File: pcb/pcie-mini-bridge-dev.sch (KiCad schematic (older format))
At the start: 20 parts, among them J1 Conn_01x02, J2 USB_C_Receptacle, J3 Conn_01x02, J4 Conn_01x02, J5 PCIe_x1, U1 TPS2594xx

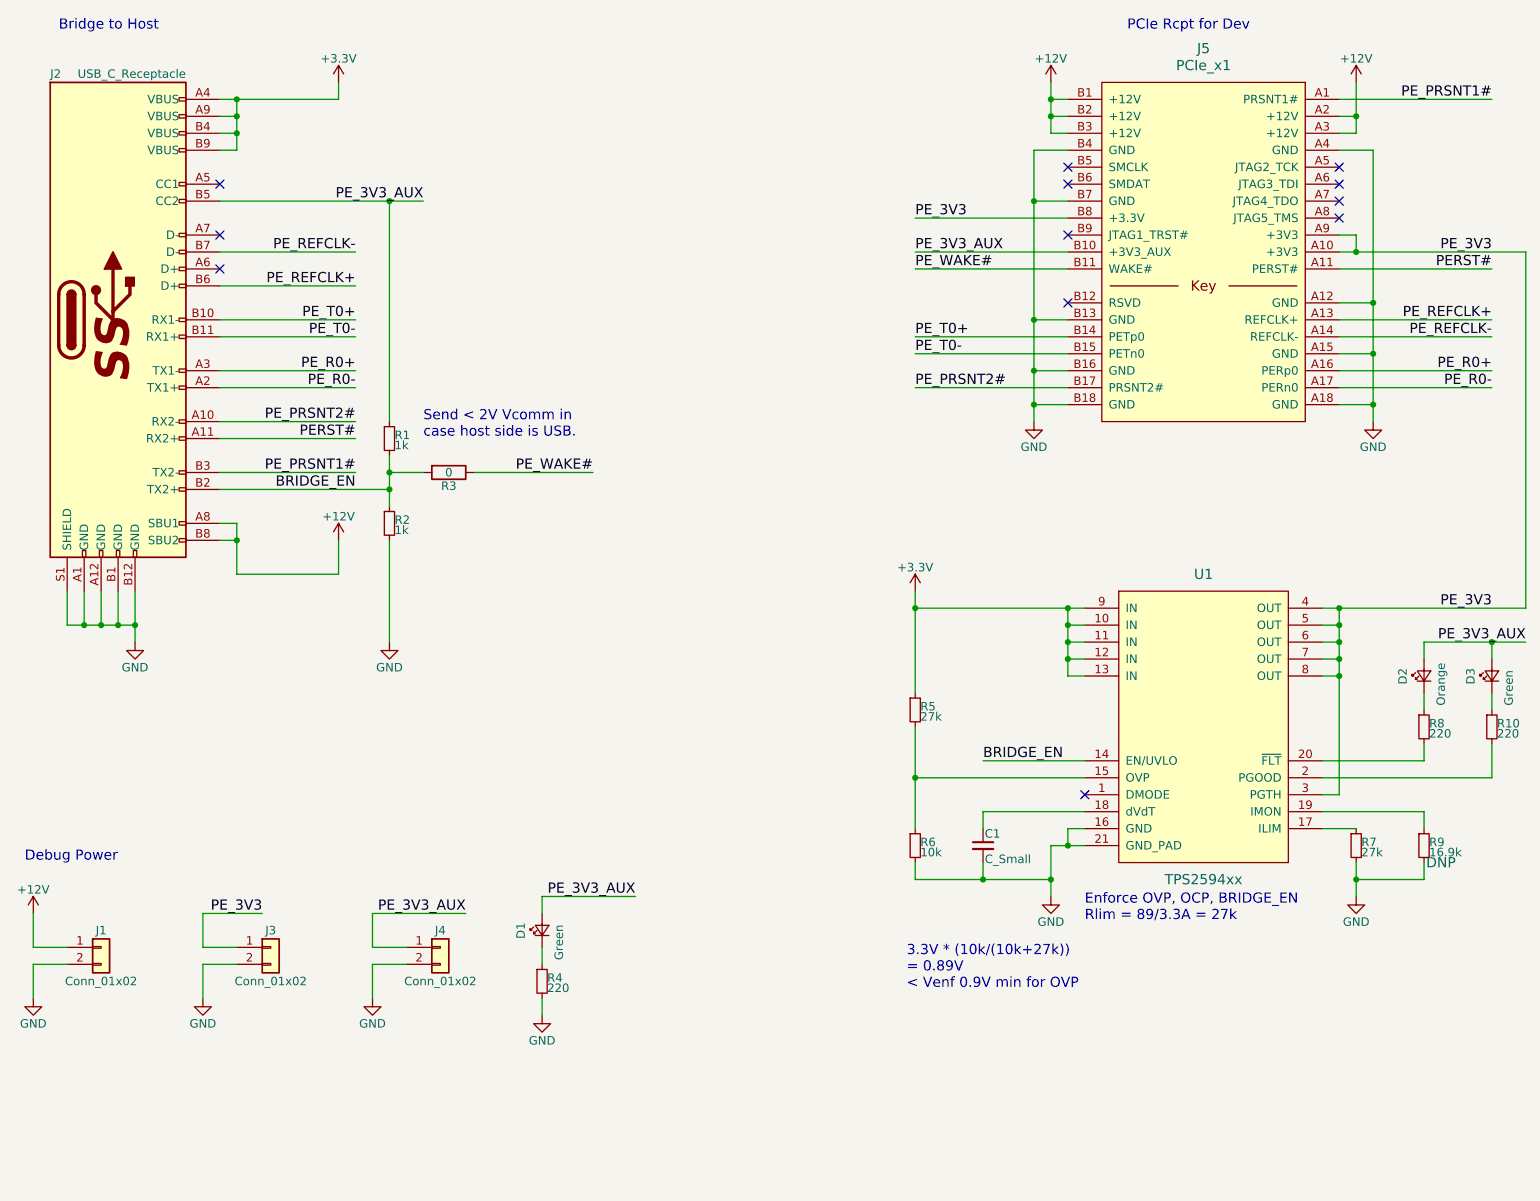
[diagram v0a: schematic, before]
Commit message: dev pcb layout, outline and hole parts
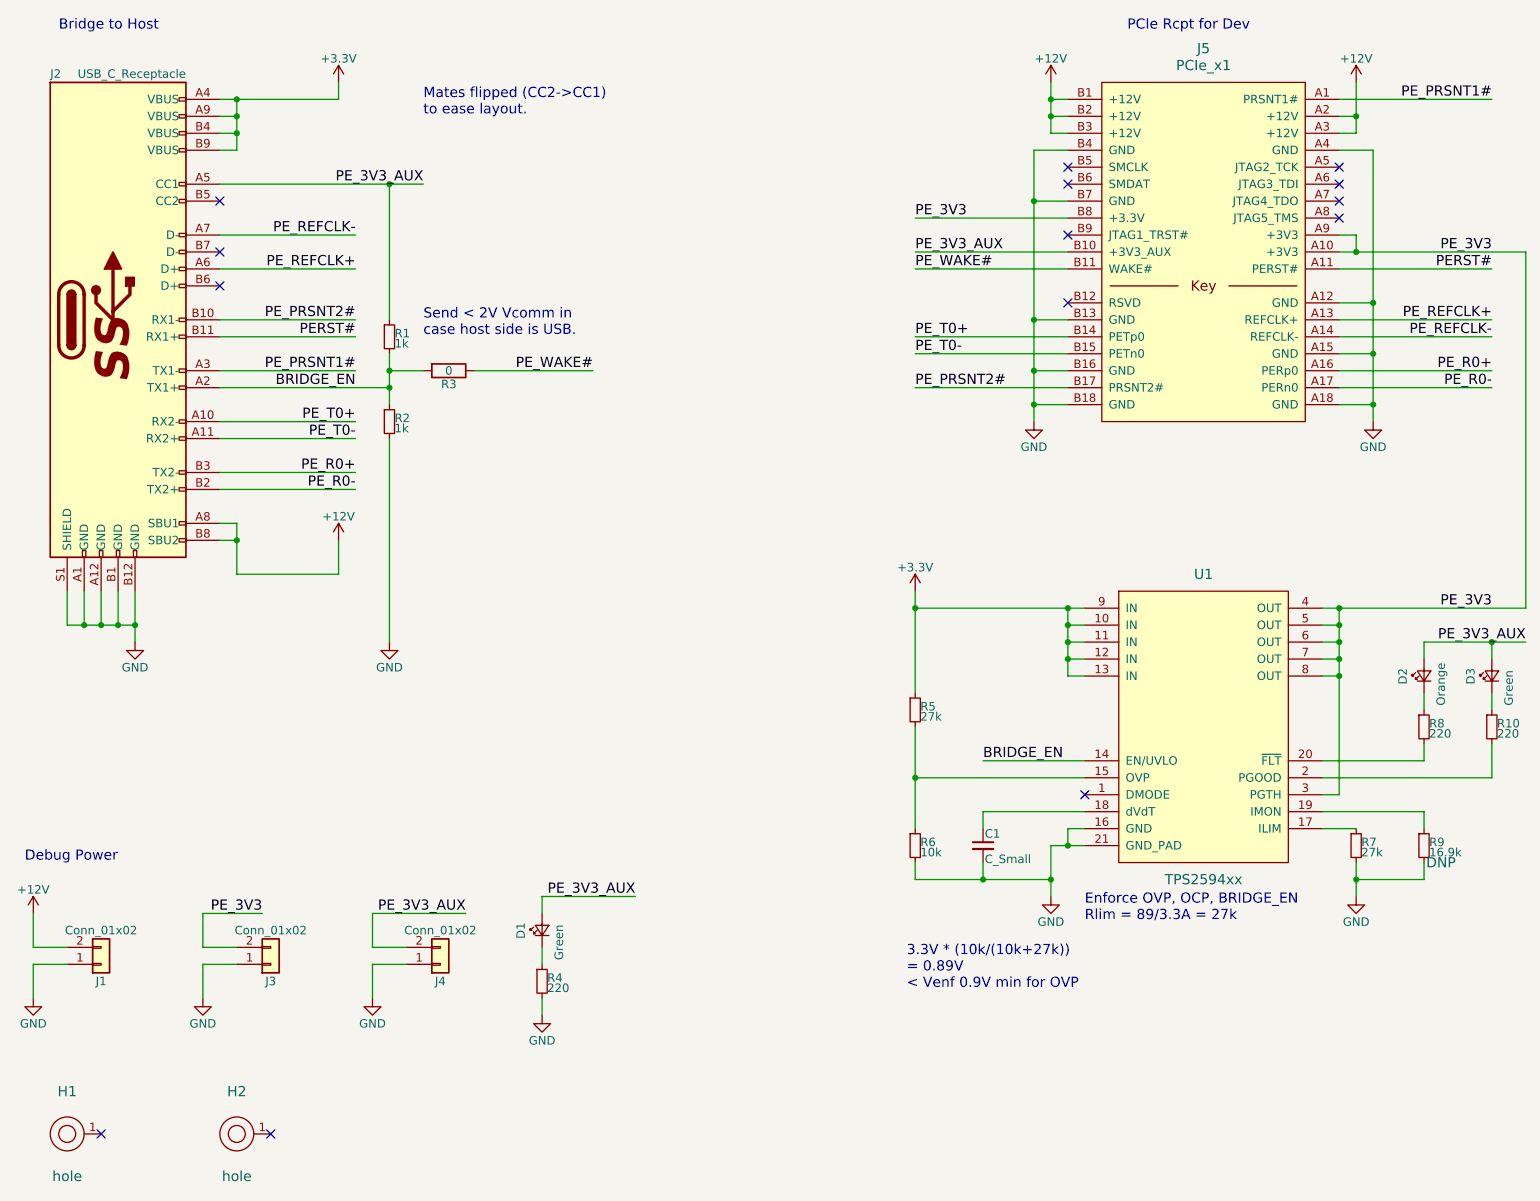
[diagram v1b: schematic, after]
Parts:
- added H1, H2: hole, pcie-mini-bridge-special:hole-m3, symbol hole
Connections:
- net +12V: now also J1.2 (Pin_2); no longer J1.1 (Pin_1)
- net BRIDGE_EN: now also J2.A2 (TX1+); no longer J2.B2 (TX2+)
- net GND: now also J1.1 (Pin_1), J3.1 (Pin_1), J4.1 (Pin_1); no longer J1.2 (Pin_2), J3.2 (Pin_2), J4.2 (Pin_2)
- net PERST#: now also J2.B11 (RX1+); no longer J2.A11 (RX2+)
- net PE_3V3: now also J3.2 (Pin_2); no longer J3.1 (Pin_1)
- net PE_3V3_AUX: now also J2.A5 (CC1), J4.2 (Pin_2); no longer J2.B5 (CC2), J4.1 (Pin_1)
- net PE_PRSNT1#: now also J2.A3 (TX1-); no longer J2.B3 (TX2-)
- net PE_PRSNT2#: now also J2.B10 (RX1-); no longer J2.A10 (RX2-)
- net PE_R0+: now also J2.B3 (TX2-); no longer J2.A3 (TX1-)
- net PE_R0-: now also J2.B2 (TX2+); no longer J2.A2 (TX1+)
- net PE_REFCLK+: now also J2.A6 (D+); no longer J2.B6 (D+)
- net PE_REFCLK-: now also J2.A7 (D-); no longer J2.B7 (D-)
- net PE_T0+: now also J2.A10 (RX2-); no longer J2.B10 (RX1-)
- net PE_T0-: now also J2.A11 (RX2+); no longer J2.B11 (RX1+)
- no-connect marks 12 -> 14
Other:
- note added: "Mates flipped (CC2->CC1)\nto ease layout."
- moved on the sheet: R1, R2, R3
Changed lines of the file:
@@
 L R_Small R1
 U 1 1 5A19B2A1
-P 3900 3100
-F 0 "R1" H 3930 3120 50  0000 L CNN
-F 1 "1k" H 3930 3060 50  0000 L CNN
-F 2 "Resistors_SMD:R_0603" H 3900 3100 50  0001 C CNN
-F 3 "" H 3900 3100 50  0001 C CNN
-	1    3900 3100
+P 3900 2500
+F 0 "R1" H 3930 2520 50  0000 L CNN
+F 1 "1k" H 3930 2460 50  0000 L CNN
+F 2 "Resistors_SMD:R_0603" H 3900 2500 50  0001 C CNN
+F 3 "" H 3900 2500 50  0001 C CNN
+	1    3900 2500
 	1    0    0    -1
 $EndComp
@@
 L Conn_01x02 J1
 U 1 1 5A19B2EB
-P 2200 6100
-F 0 "J1" H 2200 6200 50  0000 C CNN
-F 1 "Conn_01x02" H 2200 5900 50  0000 C CNN
-F 2 "Pin_Headers:Pin_Header_Straight_1x02" H 2200 6100 50  0001 C CNN
-F 3 "" H 2200 6100 50  0001 C CNN
-	1    2200 6100
-	1    0    0    -1
+P 2200 6200
+F 0 "J1" H 2200 6300 50  0000 C CNN
+F 1 "Conn_01x02" H 2200 6000 50  0000 C CNN
+F 2 "Pin_Headers:Pin_Header_Straight_1x02" H 2200 6200 50  0001 C CNN
+F 3 "" H 2200 6200 50  0001 C CNN
+	1    2200 6200
+	1    0    0    1
 $EndComp
 $Comp
 L Conn_01x02 J3
 U 1 1 5A19B340
-P 3200 6100
-F 0 "J3" H 3200 6200 50  0000 C CNN
-F 1 "Conn_01x02" H 3200 5900 50  0000 C CNN
-F 2 "Pin_Headers:Pin_Header_Straight_1x02" H 3200 6100 50  0001 C CNN
-F 3 "" H 3200 6100 50  0001 C CNN
-	1    3200 6100
-	1    0    0    -1
+P 3200 6200
+F 0 "J3" H 3200 6300 50  0000 C CNN
+F 1 "Conn_01x02" H 3200 6000 50  0000 C CNN
+F 2 "Pin_Headers:Pin_Header_Straight_1x02" H 3200 6200 50  0001 C CNN
+F 3 "" H 3200 6200 50  0001 C CNN
+	1    3200 6200
+	1    0    0    1
 $EndComp
 $Comp
 L Conn_01x02 J4
 U 1 1 5A19B377
-P 4200 6100
-F 0 "J4" H 4200 6200 50  0000 C CNN
-F 1 "Conn_01x02" H 4200 5900 50  0000 C CNN
-F 2 "Pin_Headers:Pin_Header_Straight_1x02" H 4200 6100 50  0001 C CNN
-F 3 "" H 4200 6100 50  0001 C CNN
-	1    4200 6100
-	1    0    0    -1
+P 4200 6200
+F 0 "J4" H 4200 6300 50  0000 C CNN
+F 1 "Conn_01x02" H 4200 6000 50  0000 C CNN
+F 2 "Pin_Headers:Pin_Header_Straight_1x02" H 4200 6200 50  0001 C CNN
+F 3 "" H 4200 6200 50  0001 C CNN
+	1    4200 6200
+	1    0    0    1
 $EndComp
 $Comp
@@
 $EndComp
 Wire Wire Line
-	2900 2400 3700 2400
-Wire Wire Line
-	2900 2500 3700 2500
-Text Label 3700 2500 2    60   ~ 0
+	2900 3000 3700 3000
+Wire Wire Line
+	2900 3100 3700 3100
+Text Label 3700 3100 2    60   ~ 0
 PE_T0-
-Text Label 3700 2400 2    60   ~ 0
+Text Label 3700 3000 2    60   ~ 0
 PE_T0+
-Wire Wire Line
-	2900 1700 4100 1700
-NoConn ~ 2900 1600
-Text Label 4100 1700 2    60   ~ 0
+NoConn ~ 2900 1700
+Text Label 4100 1600 2    60   ~ 0
 PE_3V3_AUX
 Text Label 4350 5900 2    60   ~ 0
@@
 $EndComp
 Wire Wire Line
+	2900 3300 3700 3300
+Wire Wire Line
+	3700 3400 2900 3400
+Text Label 3700 3400 2    60   ~ 0
+PE_R0-
+Text Label 3700 3300 2    60   ~ 0
+PE_R0+
+Wire Wire Line
+	2900 2400 3700 2400
+Wire Wire Line
+	3700 2500 2900 2500
+Text Label 3700 2700 2    60   ~ 0
+PE_PRSNT1#
+Text Label 3700 2500 2    60   ~ 0
+PERST#
+Wire Wire Line
 	2900 2700 3700 2700
-Wire Wire Line
-	3700 2800 2900 2800
+Text Label 3700 2400 2    60   ~ 0
+PE_PRSNT2#
 Text Label 3700 2800 2    60   ~ 0
-PE_R0-
-Text Label 3700 2700 2    60   ~ 0
-PE_R0+
-Wire Wire Line
-	2900 3000 3700 3000
-Wire Wire Line
-	3700 3100 2900 3100
-Text Label 3700 3300 2    60   ~ 0
-PE_PRSNT1#
-Text Label 3700 3100 2    60   ~ 0
-PERST#
-Wire Wire Line
-	2900 3300 3700 3300
-Text Label 3700 3000 2    60   ~ 0
-PE_PRSNT2#
-Text Label 3700 3400 2    60   ~ 0
 BRIDGE_EN
 $Comp
 L R R3
 U 1 1 5A19B690
-P 4250 3300
-F 0 "R3" V 4330 3300 50  0000 C CNN
-F 1 "0" V 4250 3300 50  0000 C CNN
-F 2 "Resistors_SMD:R_0603" V 4180 3300 50  0001 C CNN
-F 3 "" H 4250 3300 50  0001 C CNN
-	1    4250 3300
+P 4250 2700
+F 0 "R3" V 4330 2700 50  0000 C CNN
+F 1 "0" V 4250 2700 50  0000 C CNN
+F 2 "Resistors_SMD:R_0603" V 4180 2700 50  0001 C CNN
+F 3 "" H 4250 2700 50  0001 C CNN
+	1    4250 2700
 	0    1    1    0
 $EndComp
 Wire Wire Line
-	3900 3200 3900 3500
-Connection ~ 3900 3400
-Wire Wire Line
-	4400 3300 5100 3300
-Text Label 5100 3300 2    60   ~ 0
+	3900 2600 3900 2900
+Connection ~ 3900 2800
+Text Label 5100 2700 2    60   ~ 0
 PE_WAKE#
-Text Label 3700 2000 2    60   ~ 0
+Text Label 3700 1900 2    60   ~ 0
 PE_REFCLK-
 $Comp
 L R_Small R2
 U 1 1 5A19B974
-P 3900 3600
-F 0 "R2" H 3930 3620 50  0000 L CNN
-F 1 "1k" H 3930 3560 50  0000 L CNN
-F 2 "Resistors_SMD:R_0603" H 3900 3600 50  0001 C CNN
-F 3 "" H 3900 3600 50  0001 C CNN
-	1    3900 3600
+P 3900 3000
+F 0 "R2" H 3930 3020 50  0000 L CNN
+F 1 "1k" H 3930 2960 50  0000 L CNN
+F 2 "Resistors_SMD:R_0603" H 3900 3000 50  0001 C CNN
+F 3 "" H 3900 3000 50  0001 C CNN
+	1    3900 3000
 	1    0    0    -1
 $EndComp
@@
 $EndComp
 Wire Wire Line
-	3900 3400 2900 3400
-Wire Wire Line
-	4100 3300 3900 3300
-Connection ~ 3900 3300
-Text Notes 4100 3100 0    60   ~ 0
+	3900 2800 2900 2800
+Wire Wire Line
+	4100 2700 3900 2700
+Connection ~ 3900 2700
+Text Notes 4100 2500 0    60   ~ 0
 Send < 2V Vcomm in\ncase host side is USB.
 $Comp
@@
 Connection ~ 9500 4500
 Wire Wire Line
-	3900 4300 3900 3700
+	3900 3100 3900 4300
 Wire Wire Line
 	3800 6400 3800 6200
@@
 Debug Power
 Wire Wire Line
-	2900 2000 3700 2000
-Wire Wire Line
-	2900 2200 3700 2200
-Text Label 3700 2200 2    60   ~ 0
+	2900 1900 3700 1900
+Wire Wire Line
+	2900 2100 3700 2100
+Text Label 3700 2100 2    60   ~ 0
 PE_REFCLK+
-NoConn ~ 2900 1900
-NoConn ~ 2900 2100
-Wire Wire Line
-	3900 3000 3900 1700
-Connection ~ 3900 1700
+NoConn ~ 2900 2000
+NoConn ~ 2900 2200
+Text Notes 4100 1200 0    60   ~ 0
+Mates flipped (CC2->CC1)\nto ease layout.
+Wire Wire Line
+	4100 1600 2900 1600
+Connection ~ 3900 1600
+Wire Wire Line
+	5100 2700 4400 2700
+Wire Wire Line
+	3900 2400 3900 1600
+$Comp
+L hole H1
+U 1 1 5A28E95E
+P 2000 7200
+F 0 "H1" H 2000 7450 60  0000 C CNN
+F 1 "hole" H 2000 6950 60  0000 C CNN
+F 2 "pcie-mini-bridge-special:hole-m3" H 2000 7200 60  0001 C CNN
+F 3 "" H 2000 7200 60  0000 C CNN
+	1    2000 7200
+	1    0    0    -1
+$EndComp
+$Comp
+L hole H2
+U 1 1 5A28EAB6
+P 3000 7200
+F 0 "H2" H 3000 7450 60  0000 C CNN
+F 1 "hole" H 3000 6950 60  0000 C CNN
+F 2 "pcie-mini-bridge-special:hole-m3" H 3000 7200 60  0001 C CNN
+F 3 "" H 3000 7200 60  0000 C CNN
+	1    3000 7200
+	1    0    0    -1
+$EndComp
+NoConn ~ 3200 7200
+NoConn ~ 2200 7200
 $EndSCHEMATC

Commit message: fix pcie footprints and remove paste and update gerbers
* fix PCIe_Fingers and PCIe_SMDEdge had bottom cu with top mask/paste
* make and use PCIe_SMDEdge-NoPaste_TE_5-1734857-x
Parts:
- D1, D3: Description (none) -> LED GREEN CLEAR 0603 SMD; Digikey Part No (none) -> 160-1183-1-ND; Mfg (none) -> Lite-On Inc; Mfg Part No (none) -> LTST-C190GKT
- D2: Description (none) -> LED ORANGE CLEAR 0603 SMD; Digikey Part No (none) -> 160-1434-1-ND; Mfg (none) -> Lite-On Inc; Mfg Part No (none) -> LTST-C190KFKT
- J5: footprint pcie-mini-bridge-special:PCIe_SMDEdge_TE_5-1734857-x -> pcie-mini-bridge-special:PCIe_SMDEdge-NoPaste_TE_5-1734857-x
- R10, R4, R8: value 220 -> 1k
- U1: Description (none) -> IC PWR MGMT EFUSE 2.7-18V 20WQFN, Circuit Breaker, Latched; Digikey Part No (none) -> 296-42152-1-ND; Mfg (none) -> Texas Instruments; Mfg Part No (none) -> TPS25944LRVCR
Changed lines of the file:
@@
 F 0 "J5" H 8700 3600 60  0000 C CNN
 F 1 "PCIe_x1" H 8700 3500 60  0000 C CNN
-F 2 "pcie-mini-bridge-special:PCIe_SMDEdge_TE_5-1734857-x" H 8700 2200 60  0001 C CNN
+F 2 "pcie-mini-bridge-special:PCIe_SMDEdge-NoPaste_TE_5-1734857-x" H 8700 2200 60  0001 C CNN
 F 3 "http://www.te.com/commerce/DocumentDelivery/DDEController?Action=srchrtrv&DocNm=1734857&DocType=Customer+Drawing&DocLang=English" H 8700 2200 60  0001 C CNN
 F 4 "TE Connectivity" H 8700 2200 60  0001 C CNN "Mfg"
@@
 F 2 "Housings_DFN_QFN:QFN-20-1EP_3x4mm_Pitch0.5mm" H 8700 4700 60  0001 C CNN
 F 3 "" H 8700 4700 60  0001 C CNN
+F 4 "Texas Instruments" H 8700 4800 60  0001 C CNN "Mfg"
+F 5 "TPS25944LRVCR" H 8700 4800 60  0001 C CNN "Mfg Part No"
+F 6 "296-42152-1-ND" H 8700 4800 60  0001 C CNN "Digikey Part No"
+F 7 "IC PWR MGMT EFUSE 2.7-18V 20WQFN, Circuit Breaker, Latched" H 8700 4800 60  0001 C CNN "Description"
 	1    8700 4800
 	1    0    0    -1
@@
 P 10000 4800
 F 0 "R8" H 10030 4820 50  0000 L CNN
-F 1 "220" H 10030 4760 50  0000 L CNN
+F 1 "1k" H 10030 4760 50  0000 L CNN
 F 2 "Resistors_SMD:R_0603" H 10000 4800 50  0001 C CNN
 F 3 "" H 10000 4800 50  0001 C CNN
@@
 P 10400 4800
 F 0 "R10" H 10430 4820 50  0000 L CNN
-F 1 "220" H 10430 4760 50  0000 L CNN
+F 1 "1k" H 10430 4760 50  0000 L CNN
 F 2 "Resistors_SMD:R_0603" H 10400 4800 50  0001 C CNN
 F 3 "" H 10400 4800 50  0001 C CNN
@@
 F 2 "LEDs:LED_0603" V 10000 4500 50  0001 C CNN
 F 3 "" V 10000 4500 50  0001 C CNN
+F 4 "Lite-On Inc" H 10000 4500 60  0001 C CNN "Mfg"
+F 5 "LTST-C190KFKT" H 10000 4500 60  0001 C CNN "Mfg Part No"
+F 6 "160-1434-1-ND" H 10000 4500 60  0001 C CNN "Digikey Part No"
+F 7 "LED ORANGE CLEAR 0603 SMD" H 10000 4500 60  0001 C CNN "Description"
 	1    10000 4500
 	0    -1   -1   0
@@
 F 2 "LEDs:LED_0603" V 10400 4500 50  0001 C CNN
 F 3 "" V 10400 4500 50  0001 C CNN
+F 4 "Lite-On Inc" H 10400 4500 60  0001 C CNN "Mfg"
+F 5 "LTST-C190GKT" H 10400 4500 60  0001 C CNN "Mfg Part No"
+F 6 "160-1183-1-ND" H 10400 4500 60  0001 C CNN "Digikey Part No"
+F 7 "LED GREEN CLEAR 0603 SMD" H 10400 4500 60  0001 C CNN "Description"
 	1    10400 4500
 	0    -1   -1   0
@@
 P 4800 6300
 F 0 "R4" H 4830 6320 50  0000 L CNN
-F 1 "220" H 4830 6260 50  0000 L CNN
+F 1 "1k" H 4830 6260 50  0000 L CNN
 F 2 "Resistors_SMD:R_0603" H 4800 6300 50  0001 C CNN
 F 3 "" H 4800 6300 50  0001 C CNN
@@
 F 2 "LEDs:LED_0603" V 4800 6000 50  0001 C CNN
 F 3 "" V 4800 6000 50  0001 C CNN
+F 4 "Lite-On Inc" H 4800 6000 60  0001 C CNN "Mfg"
+F 5 "LTST-C190GKT" H 4800 6000 60  0001 C CNN "Mfg Part No"
+F 6 "160-1183-1-ND" H 4800 6000 60  0001 C CNN "Digikey Part No"
+F 7 "LED GREEN CLEAR 0603 SMD" H 4800 6000 60  0001 C CNN "Description"
 	1    4800 6000
 	0    -1   -1   0
